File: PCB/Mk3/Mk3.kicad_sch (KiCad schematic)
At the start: 42 parts, among them J1 Screw_Terminal_01x02, J10 Con12-PortA, J2 Con4-Bank, J3 Conn_01x06_Pin, J4 Con12-PortB, J5 Conn_01x32, J6 Conn_01x32, J7 Conn_01x32, J8 Conn_01x32, J9 COM: Gnd,CTS, Vcc, Tx, Rx, DTR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

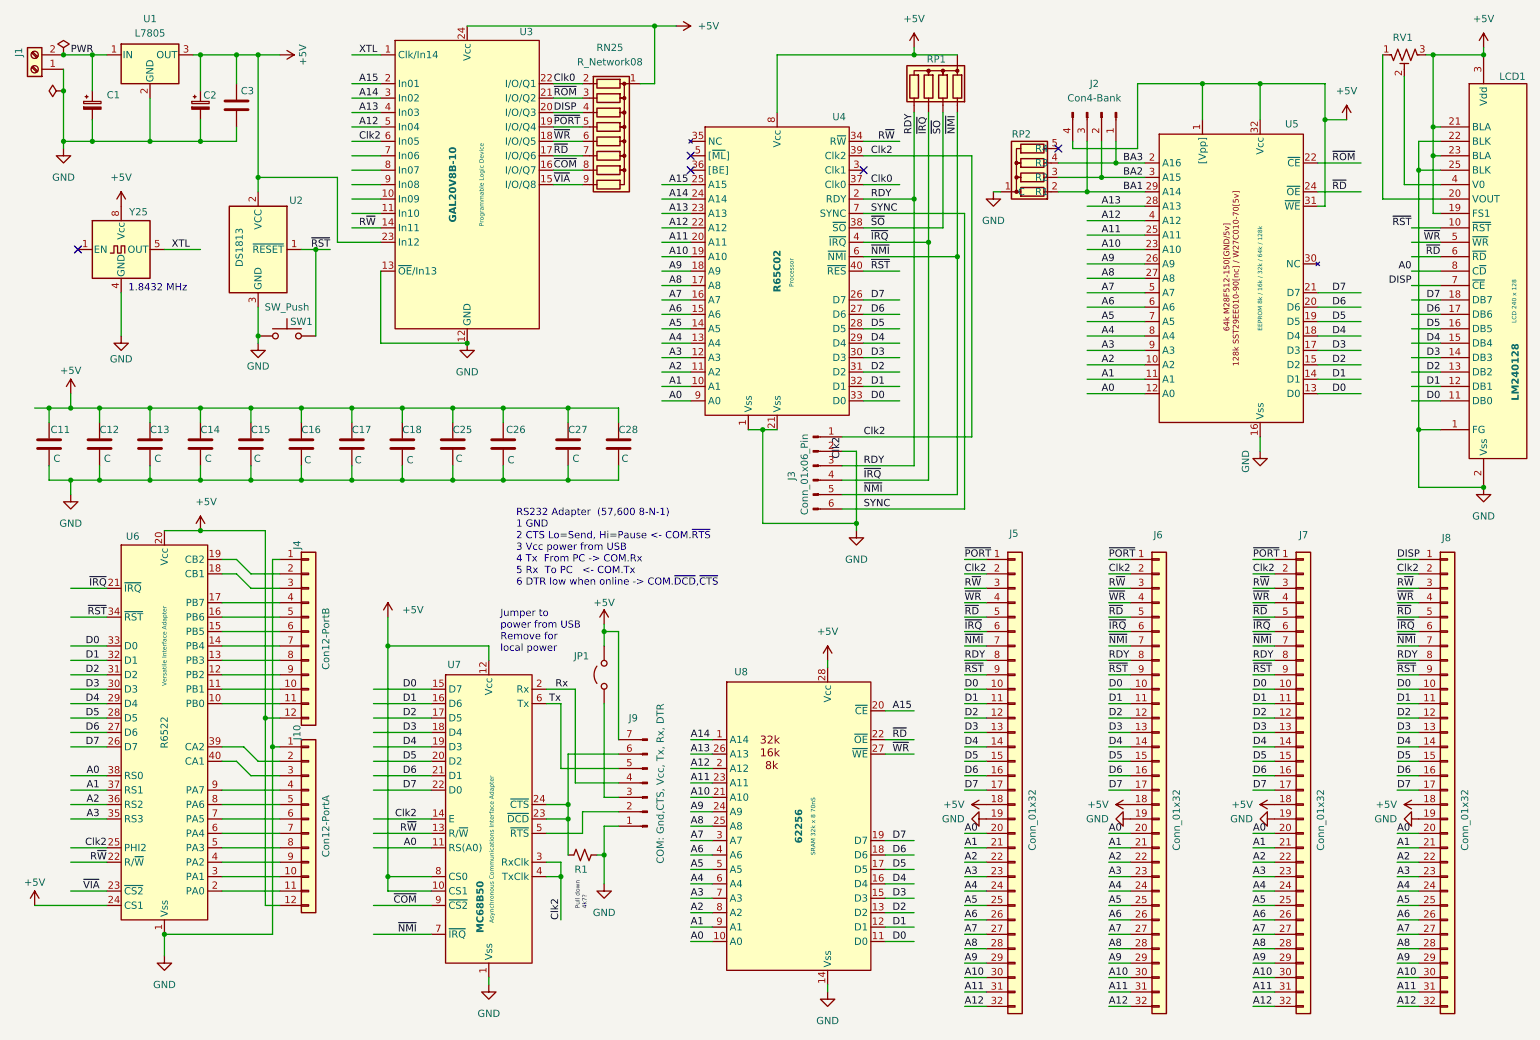
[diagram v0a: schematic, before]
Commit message: 3d model and moved trim pot
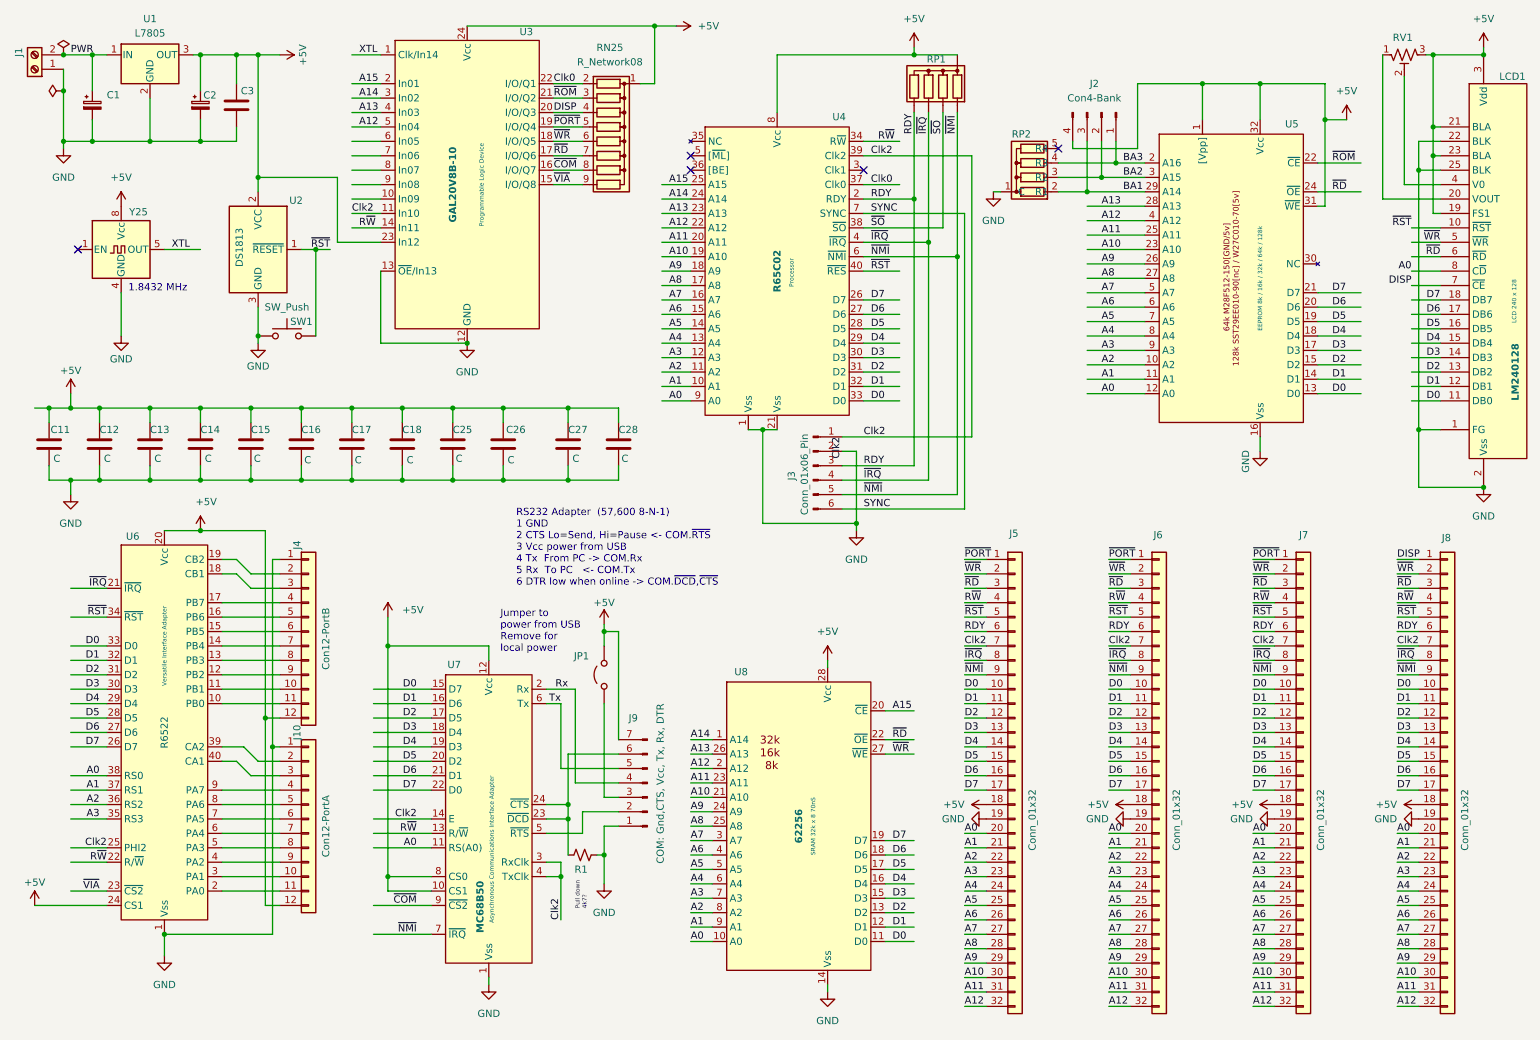
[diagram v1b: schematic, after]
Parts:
- RV1: footprint Potentiometer_THT:Potentiometer_Runtron_RM-065_Vertical -> Potentiometer_THT:Potentiometer_Piher_PT-15-V15_Vertical
- SW1: footprint Library:MiniSwitch -> Button_Switch_THT:SW_PUSH_1P1T_6x3.5mm_H4.3_APEM_MJTP1243
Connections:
- net Clk2: now also J5.7 (Pin_7), J6.7 (Pin_7), J7.7 (Pin_7), J8.7 (Pin_7), U3.11 (In10); no longer J5.2 (Pin_2), J6.2 (Pin_2), J7.2 (Pin_2), J8.2 (Pin_2), U3.6 (In05)
- net RDY: now also J5.6 (Pin_6), J6.6 (Pin_6), J7.6 (Pin_6), J8.6 (Pin_6); no longer J5.8 (Pin_8), J6.8 (Pin_8), J7.8 (Pin_8), J8.8 (Pin_8)
- net R~{W}: now also J5.4 (Pin_4), J6.4 (Pin_4), J7.4 (Pin_4), J8.4 (Pin_4); no longer J5.3 (Pin_3), J6.3 (Pin_3), J7.3 (Pin_3), J8.3 (Pin_3)
- net ~{IRQ}: now also J5.8 (Pin_8), J6.8 (Pin_8), J7.8 (Pin_8), J8.8 (Pin_8); no longer J5.6 (Pin_6), J6.6 (Pin_6), J7.6 (Pin_6), J8.6 (Pin_6)
- net ~{NMI}: now also J5.9 (Pin_9), J6.9 (Pin_9), J7.9 (Pin_9), J8.9 (Pin_9); no longer J5.7 (Pin_7), J6.7 (Pin_7), J7.7 (Pin_7), J8.7 (Pin_7)
- net ~{RD}: now also J5.3 (Pin_3), J6.3 (Pin_3), J7.3 (Pin_3), J8.3 (Pin_3); no longer J5.5 (Pin_5), J6.5 (Pin_5), J7.5 (Pin_5), J8.5 (Pin_5)
- net ~{RST}: now also J5.5 (Pin_5), J6.5 (Pin_5), J7.5 (Pin_5), J8.5 (Pin_5); no longer J5.9 (Pin_9), J6.9 (Pin_9), J7.9 (Pin_9), J8.9 (Pin_9)
- net ~{WR}: now also J5.2 (Pin_2), J6.2 (Pin_2), J7.2 (Pin_2), J8.2 (Pin_2); no longer J5.4 (Pin_4), J6.4 (Pin_4), J7.4 (Pin_4), J8.4 (Pin_4)
